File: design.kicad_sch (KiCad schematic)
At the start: 88 parts, among them J1 2601-3108, J10 Conn_01x04, J11 Conn_01x04, J12 Conn_01x03, J13 Conn_01x03, J14 BM04B-SRSS-TB_LF__SN_, J2 2601-3108, J3 2601-3108, J4 TYPE-C-31-M-12, J5 SKEDD-UPDI-4, J6 Conn_01x04, J7 Conn_01x04, J8 Conn_01x04, J9 Conn_01x04, U1 ATtiny1616-S, U2 AP2112K-3.3, U3 CP2105, U4 ATtiny1616-M

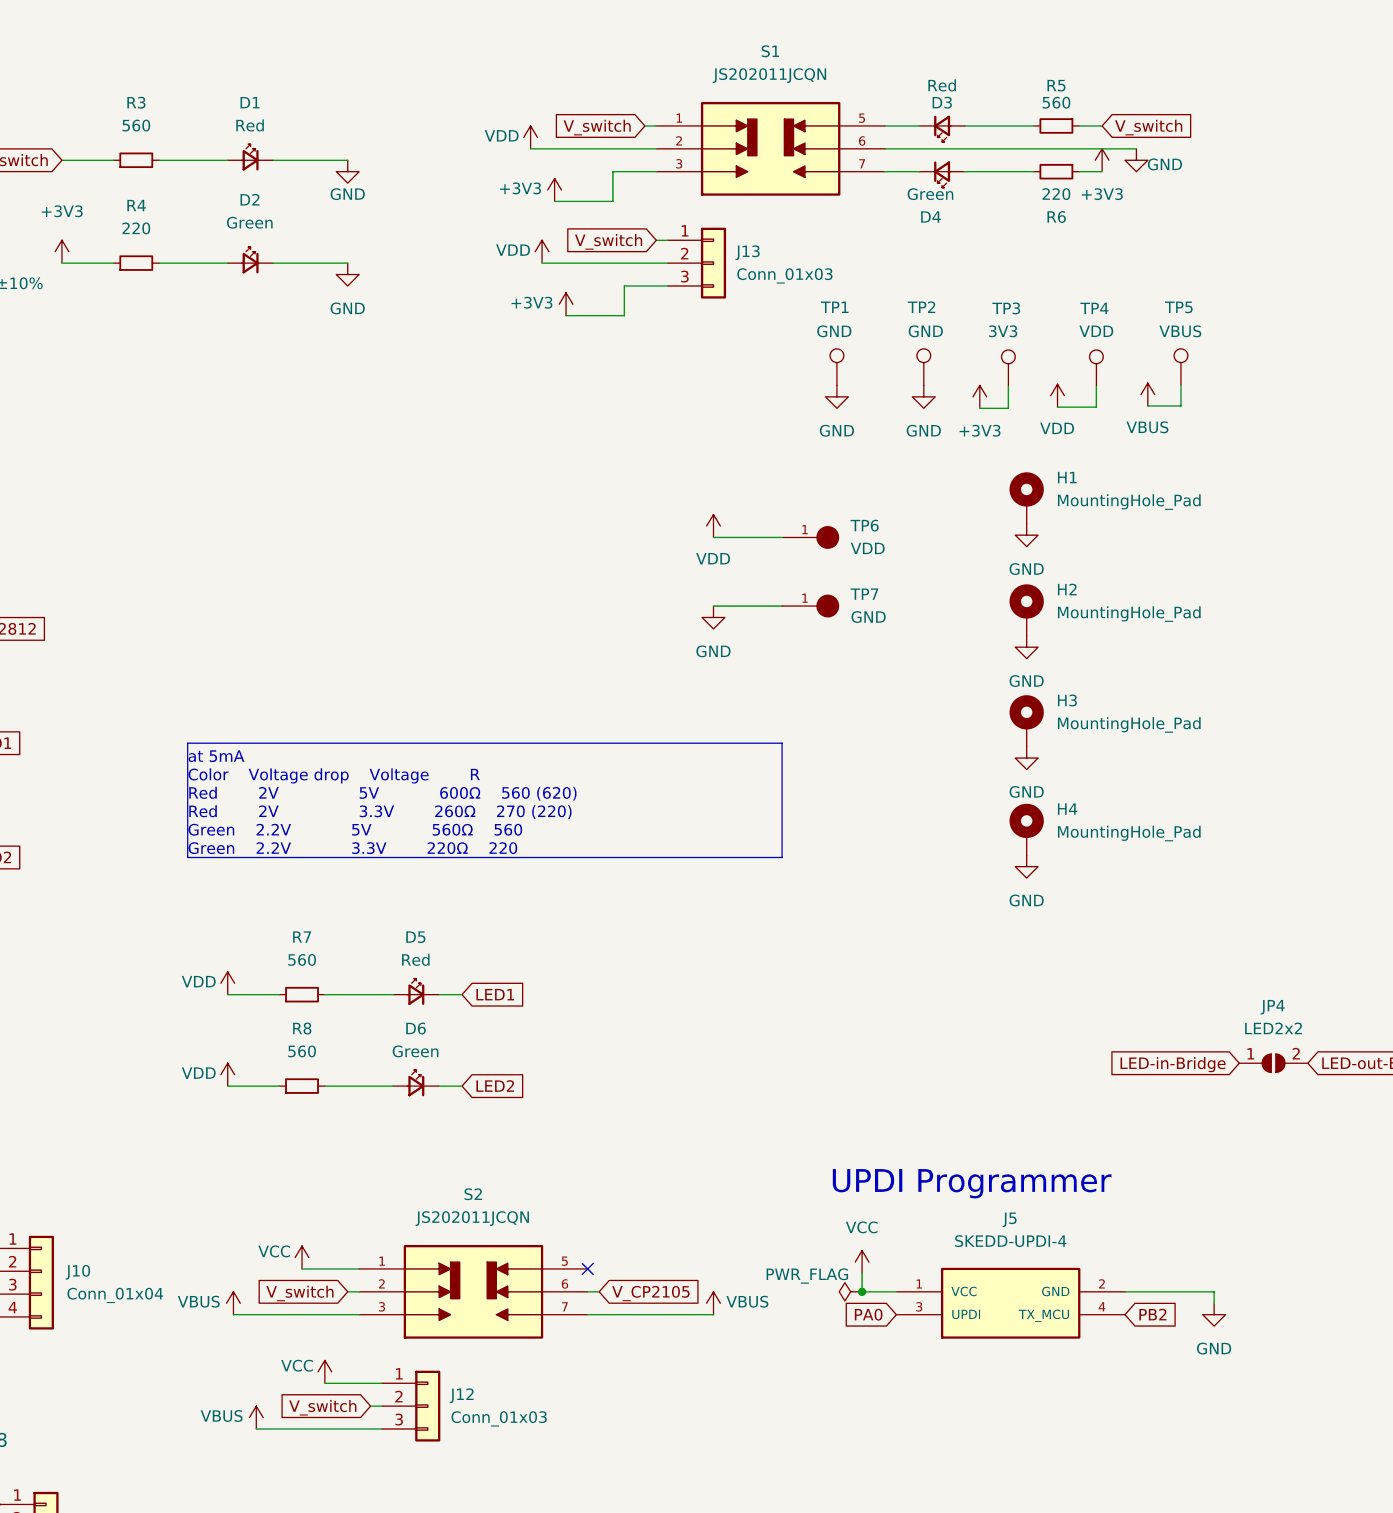
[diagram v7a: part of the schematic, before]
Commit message: change to K3-2235S-K1 / JS202011SCQN DPDT Switch
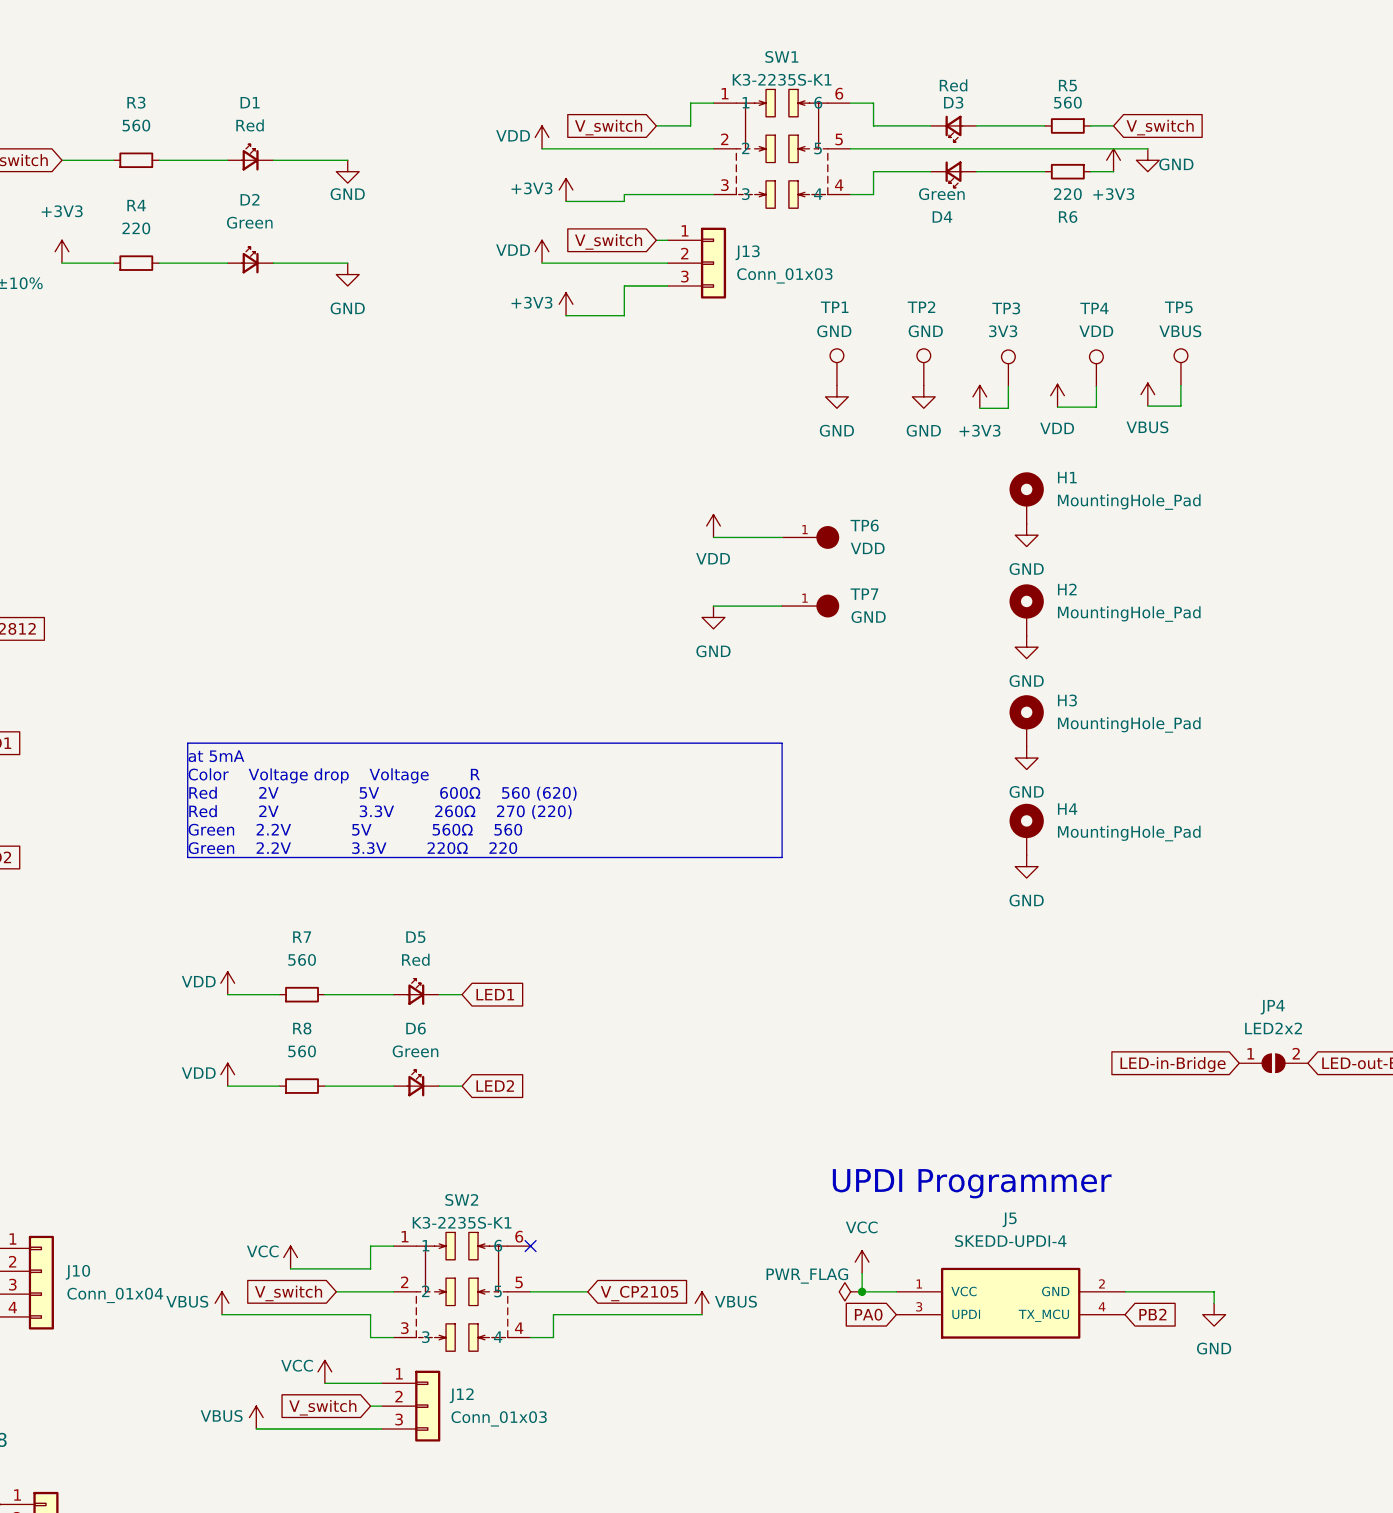
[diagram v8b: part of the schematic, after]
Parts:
- removed S1, S2: JS202011JCQN, Snapeda:SW_JS202011JCQN, symbol Snapeda:JS202011JCQN
- added SW1, SW2: K3-2235S-K1, Snapeda:easyeda2kicad_SW-SMD_K3-2235S-K1, symbol Snapeda:K3-2235S-K1
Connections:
- net +3V3: now also SW1.3
- net GND: now also SW1.5
- net VBUS: now also SW2.3, SW2.4
- net VCC: now also SW2.1
- net VDD: now also SW1.2
- net V_CP2105: now also SW2.5
- net V_switch: now also SW1.1, SW2.2
- net at D3.1 (K): now also SW1.6
- net at D4.1 (K): now also SW1.4
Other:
- moved on the sheet: D3, D4, R5, R6
